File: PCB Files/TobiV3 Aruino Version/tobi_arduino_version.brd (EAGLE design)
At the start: 103 x 74 mm, 45 parts

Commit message: first shot at positioning components
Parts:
- removed JP10, JP11, JP12, JP13, JP8, JP9: (no value), pinhead:1X03
- removed JP2, JP3, JP4, JP5, JP6, JP7: (no value), pinhead:1X02
- added M0_ENC, M1_ENC, M2_ENC, M3_ENC, M4_ENC, M5_ENC: (no value), pinhead:1X03
- added MOT_0, MOT_1, MOT_2, MOT_3, MOT_4, MOT_5: (no value), pinhead:1X02
- moved LED5 174.6 mm to (92.9, 32.7)
- moved PB_LED 166.9 mm to (84.0, 76.3)
- moved PB_SWITCH 157.2 mm to (84.0, 69.3)
- moved DRIVER1 156.7 mm to (63.5, 58.3), turned to 90 degrees
- moved R_LED5 151.2 mm to (93.4, 26.5)
- moved H4 149.6 mm to (96.0, 10.0), turned to 90 degrees
- moved POWR-PLUG 149.3 mm to (91.7, 20.4)
- moved LED3 149.2 mm to (93.2, 53.7)
- moved PCF3 144.6 mm to (84.1, 41.1)
- moved R_LED1 140.8 mm to (53.6, 76.4)
- moved R_SCL 135.4 mm to (66.7, 36.5)
- moved R_SDA 131.6 mm to (66.7, 32.5)
- moved R_LED3 128.3 mm to (93.6, 48.5)
- moved H2 120.1 mm to (96.0, 75.0)
- moved R_LED0 115.0 mm to (35.3, 76.4)
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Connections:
- new net N$1: LED0.A, R_LED0.1
- new net N$2: LED1.A, R_LED1.1
- new net N$3: LED2.A, R_LED2.1
- new net N$4: LED3.A, R_LED3.1
- new net N$5: LED4.A, R_LED4.1
- new net N$6: LED5.A, R_LED5.1
- net GND: now also M0_ENC.2, M1_ENC.2, M2_ENC.2, M3_ENC.2, M4_ENC.2, M5_ENC.2; no longer JP10.2, JP11.2, JP12.2, JP13.2, JP8.2, JP9.2
- net M0_A: now also MOT_0.1; no longer JP2.1
- net M0_B: now also MOT_0.2; no longer JP2.2
- net M0_ENC: now also M0_ENC.3; no longer JP8.3
- net M1_A: now also MOT_1.1; no longer JP3.1
- net M1_B: now also MOT_1.2; no longer JP3.2
- net M1_ENC: now also M1_ENC.3; no longer JP9.3
- net M2_A: now also MOT_2.1; no longer JP4.1
- net M2_B: now also MOT_2.2; no longer JP4.2
- net M2_ENC: now also M2_ENC.3; no longer JP10.3
- net M3_A: now also MOT_3.1; no longer JP5.1
- net M3_B: now also MOT_3.2; no longer JP5.2
- net M3_ENC: now also M3_ENC.3; no longer JP11.3
- net M4_A: now also MOT_4.1; no longer JP6.1
- net M4_B: now also MOT_4.2; no longer JP6.2
- net M4_ENC: now also M4_ENC.3; no longer JP12.3
- net M5_A: now also MOT_5.1; no longer JP7.1
- net M5_B: now also MOT_5.2; no longer JP7.2
- net M5_ENC: now also M5_ENC.3; no longer JP13.3
- net VCC: now also M0_ENC.1, M1_ENC.1, M2_ENC.1, M3_ENC.1, M4_ENC.1, M5_ENC.1; no longer JP10.1, JP11.1, JP12.1, JP13.1, JP8.1, JP9.1

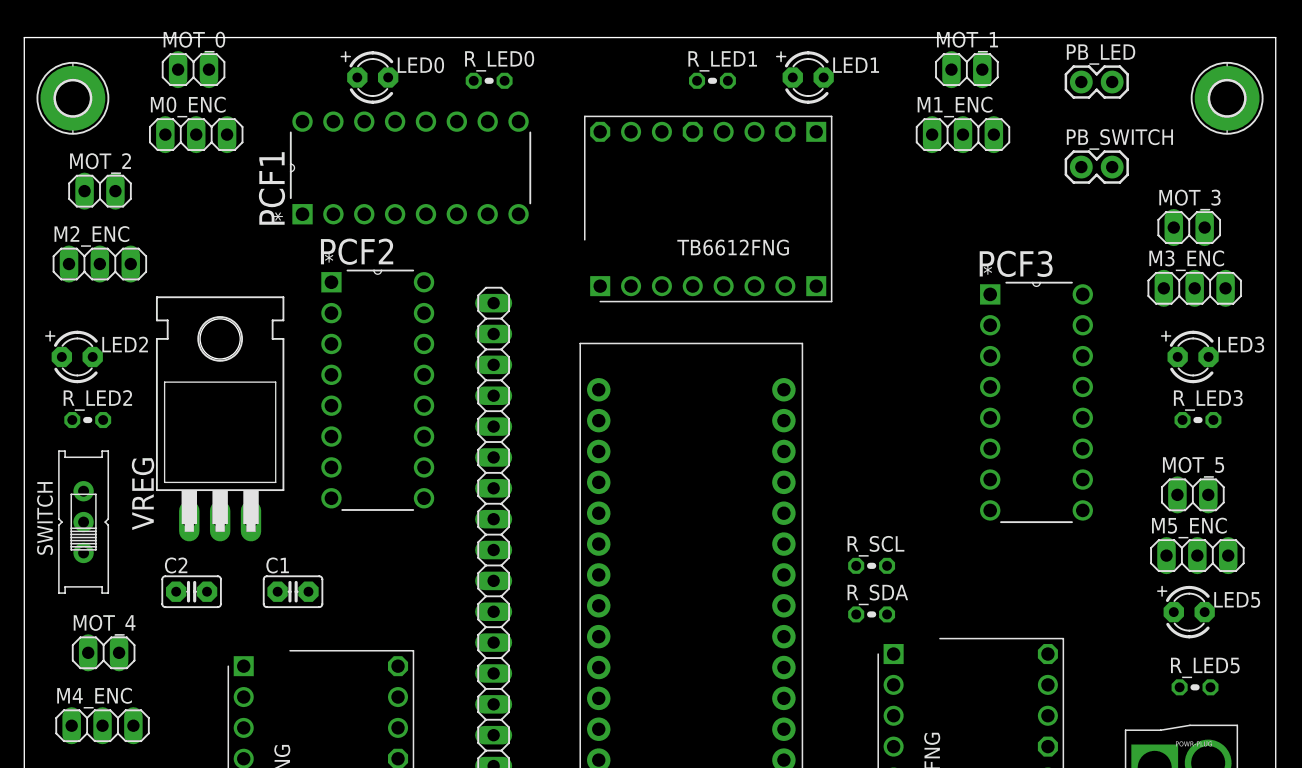
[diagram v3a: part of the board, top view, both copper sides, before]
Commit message: fix a few things on the silkscreen
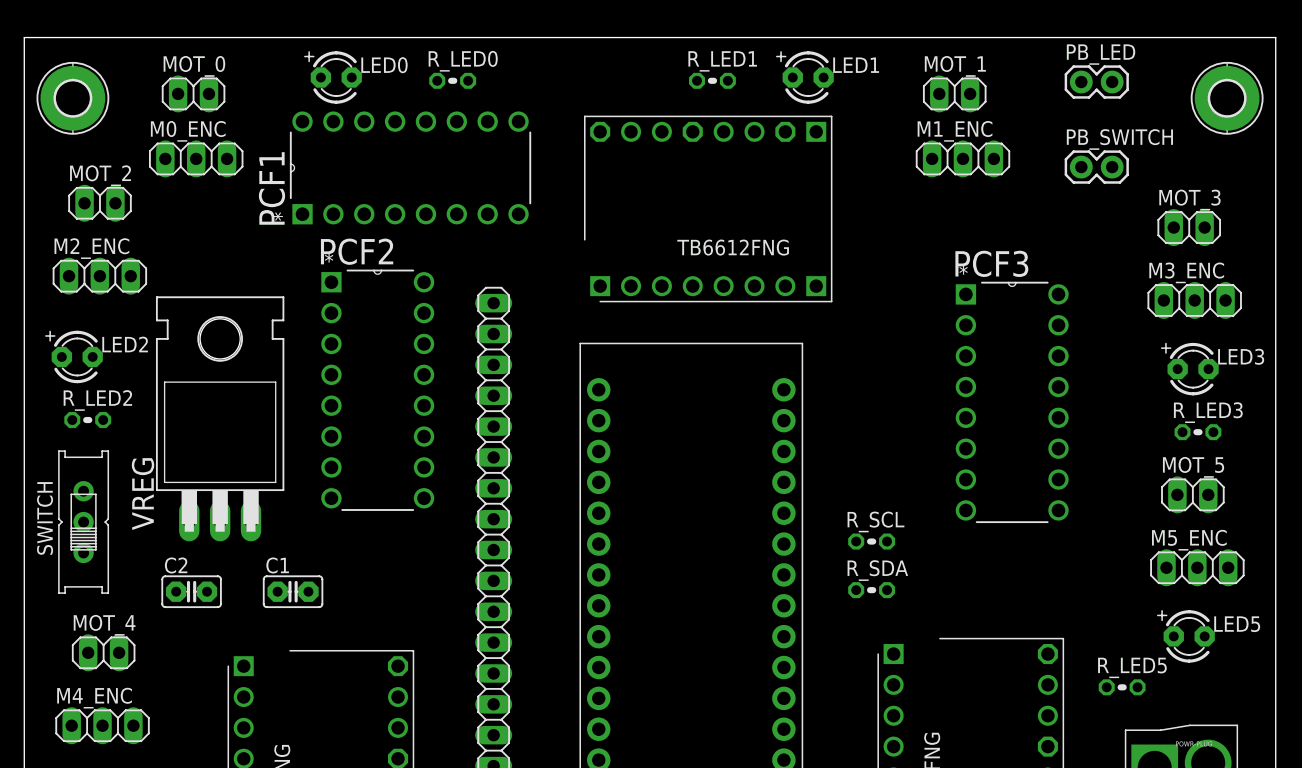
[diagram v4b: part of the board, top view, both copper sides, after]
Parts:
- moved R_LED5 6.00 mm to (87.4, 26.5)
- moved LED0 3.00 mm to (22.7, 76.7)
- moved R_LED0 3.00 mm to (32.3, 76.4)
- moved MOT_1 2.24 mm to (73.6, 75.4)
- moved LED5 2.00 mm to (92.9, 30.7)
- moved M0_ENC 2.00 mm to (11.2, 70.0)
- moved M1_ENC 2.00 mm to (74.3, 70.0)
- moved MOT_0 2.00 mm to (10.9, 75.4)
- moved PCF3 2.00 mm to (82.1, 41.1)
- moved R_SCL 2.00 mm to (66.7, 38.5)
- moved R_SDA 2.00 mm to (66.7, 34.5)
- moved LED3 1.00 mm to (93.2, 52.7)
- moved M2_ENC 1.00 mm to (3.22, 60.4)
- moved M3_ENC 1.00 mm to (93.3, 58.4)
- moved M5_ENC 1.00 mm to (93.5, 36.4)
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
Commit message: reconciled some nets
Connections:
- removed net V_IN: POWR-PLUG.POW
- net V_MOT: now also POWR-PLUG.POW

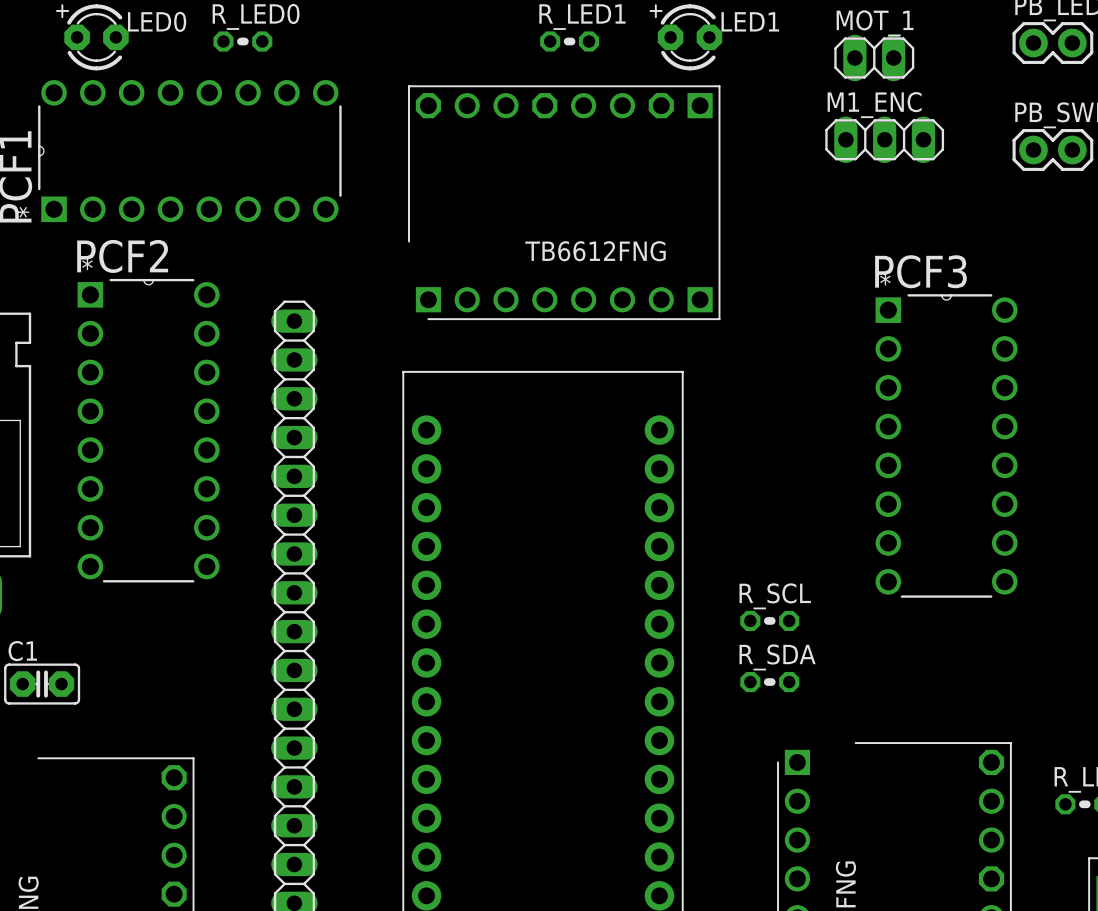
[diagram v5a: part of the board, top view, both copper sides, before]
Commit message: manual routing for scl/sda lines
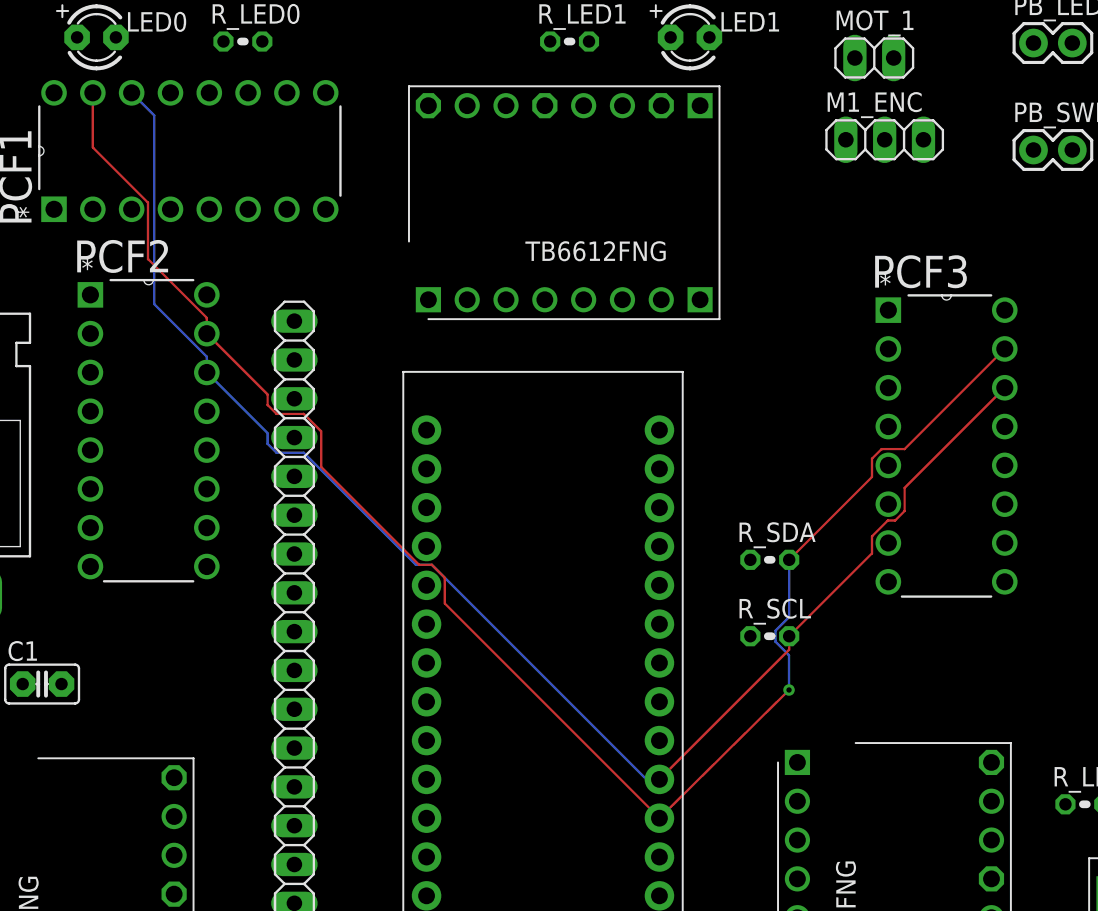
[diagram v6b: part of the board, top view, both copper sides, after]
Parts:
- moved R_SDA 8.00 mm to (66.7, 42.5)
- moved R_SCL 1.00 mm to (66.7, 37.5)
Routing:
- net SDA: track 0.00 -> 106.1 mm, vias 0 -> 1
- net SCL: track 0.00 -> 96.7 mm
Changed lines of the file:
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@@
 <element name="R_LED4" library="resistor" library_urn="urn:adsk.eagle:library:348" package="0204V" value="" x="7.98" y="14.52"/>
 <element name="R_LED5" library="resistor" library_urn="urn:adsk.eagle:library:348" package="0204V" value="" x="87.36" y="26.52"/>
-<element name="R_SCL" library="resistor" library_urn="urn:adsk.eagle:library:348" package="0204V" value="" x="66.74" y="38.52"/>
-<element name="R_SDA" library="resistor" library_urn="urn:adsk.eagle:library:348" package="0204V" value="" x="66.74" y="34.52"/>
+<element name="R_SCL" library="resistor" library_urn="urn:adsk.eagle:library:348" package="0204V" value="" x="66.74" y="37.52"/>
+<element name="R_SDA" library="resistor" library_urn="urn:adsk.eagle:library:348" package="0204V" value="" x="66.74" y="42.52"/>
 <element name="SWITCH" library="adafruit" package="EG1218" value="" x="1.88" y="40.12" rot="R90"/>
 <element name="VREG" library="adafruit" package="TO220H" value="7805T" x="13.12" y="50.37"/>
@@
 <wire x1="74.5" y1="56.32" x2="82.12" y2="58.86" width="0" layer="19" extent="1-1"/>
 <wire x1="71.72" y1="70.01" x2="74.5" y2="56.32" width="0" layer="19" extent="1-1"/>
-<wire x1="65.47" y1="38.52" x2="74.5" y2="56.32" width="0" layer="19" extent="1-1"/>
-<wire x1="65.47" y1="34.52" x2="65.47" y2="38.52" width="0" layer="19" extent="1-1"/>
-<wire x1="68.55" y1="26.72" x2="65.47" y2="34.52" width="0" layer="19" extent="1-1"/>
+<wire x1="65.47" y1="37.52" x2="74.5" y2="56.32" width="0" layer="19" extent="1-1"/>
+<wire x1="65.47" y1="42.52" x2="65.47" y2="37.52" width="0" layer="19" extent="1-1"/>
+<wire x1="68.55" y1="26.72" x2="65.47" y2="42.52" width="0" layer="19" extent="1-1"/>
 <wire x1="91.01" y1="36.36" x2="90.79" y2="58.36" width="0" layer="19" extent="1-1"/>
 <wire x1="46.94" y1="59.54" x2="71.72" y2="70.01" width="0" layer="19" extent="1-1"/>
@@
 <contactref element="R_SCL" pad="2"/>
 <contactref element="PCF3" pad="14"/>
-<wire x1="68.01" y1="38.52" x2="82.12" y2="53.78" width="0" layer="19" extent="1-1"/>
-<wire x1="59.52" y1="28.15" x2="68.01" y2="38.52" width="0" layer="19" extent="1-1"/>
-<wire x1="29.9" y1="54.78" x2="59.52" y2="28.15" width="0" layer="19" extent="1-1"/>
-<wire x1="24.98" y1="73.08" x2="29.9" y2="54.78" width="0" layer="19" extent="1-1"/>
+<wire x1="59.52" y1="28.15" x2="68.01" y2="36.64" width="0.1524" layer="1"/>
+<wire x1="68.01" y1="36.64" x2="68.01" y2="37.52" width="0.1524" layer="1"/>
+<wire x1="74.9418875" y1="45.0932" x2="75.5668" y2="45.7181125" width="0.1524" layer="1"/>
+<wire x1="68.01" y1="37.52" x2="73.4332" y2="42.9432" width="0.1524" layer="1"/>
+<wire x1="73.4332" y1="42.9432" x2="73.4332" y2="44.0618875" width="0.1524" layer="1"/>
+<wire x1="75.5668" y1="45.7181125" x2="75.5668" y2="47.2268" width="0.1524" layer="1"/>
+<wire x1="75.5668" y1="47.2268" x2="82.12" y2="53.78" width="0.1524" layer="1"/>
+<wire x1="73.4332" y1="44.0618875" x2="74.4645125" y2="45.0932" width="0.1524" layer="1"/>
+<wire x1="74.4645125" y1="45.0932" x2="74.9418875" y2="45.0932" width="0.1524" layer="1"/>
+<wire x1="34.457675" y1="49.5294" x2="33.8774" y2="50.109675" width="0.1524" layer="16"/>
+<wire x1="59.52" y1="28.15" x2="58.66829375" y2="28.15" width="0.1524" layer="16"/>
+<wire x1="33.8774" y1="50.109675" x2="33.8774" y2="50.8026" width="0.1524" layer="16"/>
+<wire x1="33.8774" y1="50.8026" x2="29.9" y2="54.78" width="0.1524" layer="16"/>
+<wire x1="58.66829375" y1="28.15" x2="44.62209375" y2="42.1962" width="0.1524" layer="16"/>
+<wire x1="44.62209375" y1="42.1962" x2="43.576725" y2="42.1962" width="0.1524" layer="16"/>
+<wire x1="43.576725" y1="42.1962" x2="36.243525" y2="49.5294" width="0.1524" layer="16"/>
+<wire x1="36.243525" y1="49.5294" x2="34.457675" y2="49.5294" width="0.1524" layer="16"/>
+<wire x1="29.9" y1="54.78" x2="29.9" y2="55.8113125" width="0.1524" layer="16"/>
+<wire x1="26.4532" y1="71.6068" x2="24.98" y2="73.08" width="0.1524" layer="16"/>
+<wire x1="29.9" y1="55.8113125" x2="26.4532" y2="59.2581125" width="0.1524" layer="16"/>
+<wire x1="26.4532" y1="59.2581125" x2="26.4532" y2="71.6068" width="0.1524" layer="16"/>
 </signal>
 <signal name="SDA">
@@
 <contactref element="R_SDA" pad="2"/>
 <contactref element="PCF3" pad="15"/>
-<wire x1="68.01" y1="34.52" x2="82.12" y2="56.32" width="0" layer="19" extent="1-1"/>
-<wire x1="59.52" y1="25.61" x2="68.01" y2="34.52" width="0" layer="19" extent="1-1"/>
-<wire x1="29.9" y1="57.32" x2="59.52" y2="25.61" width="0" layer="19" extent="1-1"/>
-<wire x1="22.44" y1="73.08" x2="29.9" y2="57.32" width="0" layer="19" extent="1-1"/>
+<wire x1="59.52" y1="25.61" x2="68" y2="34" width="0.1524" layer="1"/>
+<via x="68" y="34" extent="1-16" drill="0.35"/>
+<wire x1="67.121" y1="37.1517625" x2="67.121" y2="37.8882375" width="0.1524" layer="16"/>
+<wire x1="68" y1="34" x2="68" y2="36.2727625" width="0.1524" layer="16"/>
+<wire x1="68.01" y1="38.7772375" x2="68.01" y2="42.52" width="0.1524" layer="16"/>
+<wire x1="68" y1="36.2727625" x2="67.121" y2="37.1517625" width="0.1524" layer="16"/>
+<wire x1="67.121" y1="37.8882375" x2="68.01" y2="38.7772375" width="0.1524" layer="16"/>
+<wire x1="73.4332" y1="49.1418875" x2="74.0581125" y2="49.7668" width="0.1524" layer="1"/>
+<wire x1="68.01" y1="42.52" x2="73.4332" y2="47.9432" width="0.1524" layer="1"/>
+<wire x1="75.5668" y1="49.7668" x2="82.12" y2="56.32" width="0.1524" layer="1"/>
+<wire x1="73.4332" y1="47.9432" x2="73.4332" y2="49.1418875" width="0.1524" layer="1"/>
+<wire x1="74.0581125" y1="49.7668" x2="75.5668" y2="49.7668" width="0.1524" layer="1"/>
+<wire x1="34.457675" y1="52.0694" x2="33.8774" y2="52.649675" width="0.1524" layer="1"/>
+<wire x1="59.52" y1="25.61" x2="45.4738" y2="39.6562" width="0.1524" layer="1"/>
+<wire x1="45.4738" y1="39.6562" x2="45.4738" y2="41.34449375" width="0.1524" layer="1"/>
+<wire x1="33.8774" y1="52.649675" x2="33.8774" y2="53.3426" width="0.1524" layer="1"/>
+<wire x1="33.8774" y1="53.3426" x2="29.9" y2="57.32" width="0.1524" layer="1"/>
+<wire x1="45.4738" y1="41.34449375" x2="44.62209375" y2="42.1962" width="0.1524" layer="1"/>
+<wire x1="44.62209375" y1="42.1962" x2="43.78550625" y2="42.1962" width="0.1524" layer="1"/>
+<wire x1="43.78550625" y1="42.1962" x2="37.3826" y2="48.59910625" width="0.1524" layer="1"/>
+<wire x1="37.3826" y1="48.59910625" x2="37.3826" y2="50.930325" width="0.1524" layer="1"/>
+<wire x1="37.3826" y1="50.930325" x2="36.243525" y2="52.0694" width="0.1524" layer="1"/>
+<wire x1="36.243525" y1="52.0694" x2="34.457675" y2="52.0694" width="0.1524" layer="1"/>
+<wire x1="29.9" y1="57.32" x2="29.9" y2="58.3513125" width="0.1524" layer="1"/>
+<wire x1="26.0468" y1="65.9018875" x2="22.44" y2="69.5086875" width="0.1524" layer="1"/>
+<wire x1="22.44" y1="69.5086875" x2="22.44" y2="73.08" width="0.1524" layer="1"/>
+<wire x1="29.9" y1="58.3513125" x2="26.0468" y2="62.2045125" width="0.1524" layer="1"/>
+<wire x1="26.0468" y1="62.2045125" x2="26.0468" y2="65.9018875" width="0.1524" layer="1"/>
 </signal>
 <signal name="M0_IN2">
